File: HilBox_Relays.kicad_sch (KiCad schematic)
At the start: 49 parts, among them J9 Conn_01x10_Pin, K1 G5NB, K2 G5NB, K3 G5NB, K4 G5NB, K5 G5NB, Q10 BC847BS, Q11 BC847BS, Q12 BC847BS, Q8 BC847BS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

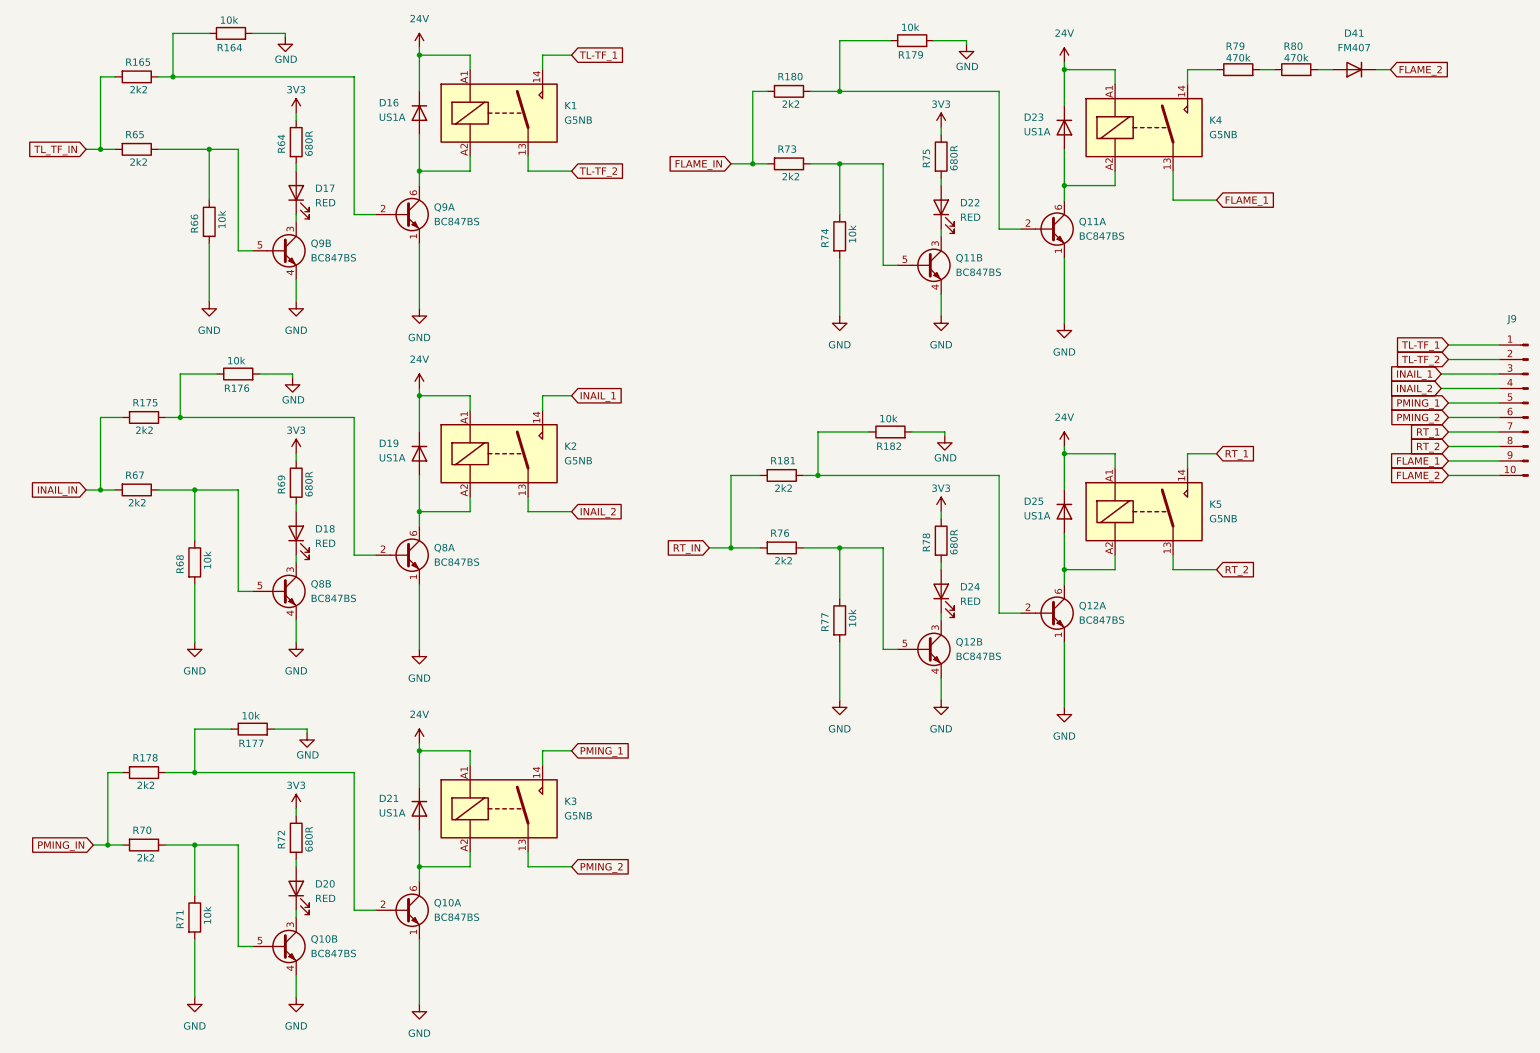
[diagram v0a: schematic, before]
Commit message: Modification in half of target
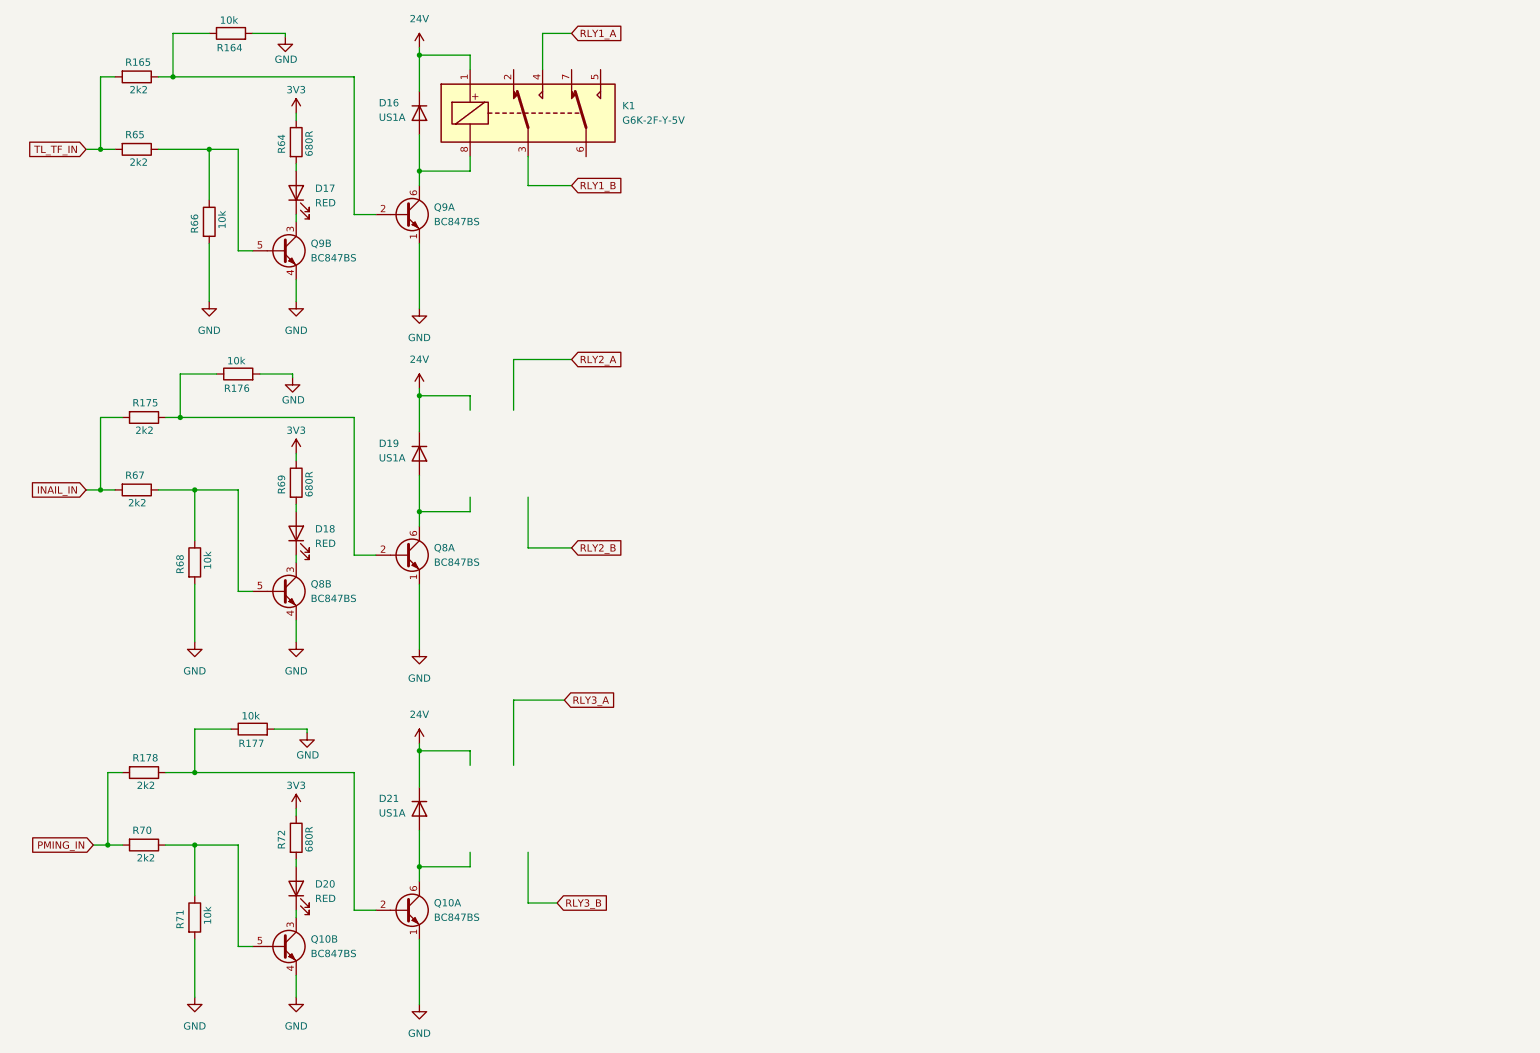
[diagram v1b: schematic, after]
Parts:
- removed D22, D24: RED, LED_SMD:LED_1206_3216Metric, symbol Device:LED
- removed D23, D25: US1A, Diode_SMD:D_SMA, symbol Diode:US1A
- removed D41: FM407, Diode_SMD:D_SMA, symbol Device:D
- removed J9: Conn_01x10_Pin, Gascard_Lib:Terminal_Block_3_81_10p, symbol Connector:Conn_01x10_Pin
- removed K1, K2, K3, K4, K5: G5NB, Relay_THT:Relay_SPST_Omron_G5NB, symbol Relay:G5NB
- removed Q11, Q12: BC847BS, Package_TO_SOT_SMD:SOT-363_SC-70-6, symbol Transistor_BJT:BC847BS
- removed R179, R182, R74, R77: 10k, Resistor_SMD:R_0603_1608Metric, symbol Device:R
- removed R180, R181, R73, R76: 2k2, Resistor_SMD:R_0603_1608Metric, symbol Device:R
- removed R75, R78: 680R, Resistor_SMD:R_0603_1608Metric, symbol Device:R
- removed R79, R80: 470k, Resistor_SMD:R_1206_3216Metric, symbol Device:R
- added K1: G6K-2F-Y-5V, Relays:RELAY_G6K-2F_DC5, symbol Relay:G6K-2
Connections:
- net 24V: now also K1.1
- net at D16.2 (A), Q9.6 (C1): now also K1.8
- new net RLY1_A: K1.4
- new net RLY1_B: K1.3

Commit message: Schematic design at finish
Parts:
- added K2, K3: G6K-2F-Y-5V, Relays:RELAY_G6K-2F_DC5, symbol Relay:G6K-2
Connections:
- net 24V: now also K2.1, K3.1
- net RLY2_A: now also K2.2
- net RLY2_B: now also K2.3
- net RLY3_A: now also K3.2
- net RLY3_B: now also K3.3
- net at D19.2 (A), Q8.6 (C1): now also K2.8
- net at D21.2 (A), Q10.6 (C1): now also K3.8
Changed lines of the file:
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@@
+	)
+	(symbol
+		(lib_id "Relay:G6K-2")
+		(at 100.33 90.17 0)
+		(unit 1)
+		(exclude_from_sim no)
+		(in_bom yes)
+		(on_board yes)
+		(dnp no)
+		(fields_autoplaced yes)
+		(property "Reference" "K2"
+			(at 116.84 88.8999 0)
+			(effects
+				(font
+					(size 1.27 1.27)
+				)
+				(justify left)
+			)
+		)
+		(property "Value" "G6K-2F-Y-5V"
+			(at 116.84 91.4399 0)
+			(effects
+				(font
+					(size 1.27 1.27)
+				)
+				(justify left)
+			)
+		)
+		(property "Footprint" "Relays:RELAY_G6K-2F_DC5"
+			(at 100.33 90.17 0)
+			(effects
+				(font
+					(size 1.27 1.27)
+				)
+				(justify left)
+				(hide yes)
+			)
+		)
+		(property "Datasheet" "http://omronfs.omron.com/en_US/ecb/products/pdf/en-g6k.pdf"
+			(at 100.33 90.17 0)
+			(effects
+				(font
+					(size 1.27 1.27)
+				)
+				(hide yes)
+			)
+		)
+		(property "Description" "Miniature 2-pole relay, Single-side Stable"
+			(at 100.33 90.17 0)
+			(effects
+				(font
+					(size 1.27 1.27)
+				)
+				(hide yes)
+			)
+		)
+		(property "JLC_PN" "C2906368"
+			(at 100.33 90.17 0)
+			(effects
+				(font
+					(size 1.27 1.27)
+				)
+				(hide yes)
+			)
+		)
+		(pin "2"
+		)
+		(pin "3"
+		)
+		(pin "1"
+		)
+		(pin "7"
+		)
+		(pin "8"
+		)
+		(pin "4"
+		)
+		(pin "6"
+		)
+		(pin "5"
+		)
+		(instances
+			(project "HilBox"
+				(path "/c950b3bb-3e52-4d0d-8bbf-240895efa80b/f996dd68-0c02-4f61-a894-5fc7c316be5e"
+					(reference "K2")
+					(unit 1)
+				)
+			)
+		)
 	)
 	(symbol
@@
 					(unit 1)
 				)
+			)
+		)
+	)
+	(symbol
+		(lib_id "Relay:G6K-2")
+		(at 100.33 152.4 0)
+		(unit 1)
+		(exclude_from_sim no)
+		(in_bom yes)
+		(on_board yes)
+		(dnp no)
+		(fields_autoplaced yes)
+		(property "Reference" "K3"
+			(at 116.84 151.1299 0)
+			(effects
+				(font
+					(size 1.27 1.27)
+				)
+				(justify left)
+			)
+		)
+		(property "Value" "G6K-2F-Y-5V"
+			(at 116.84 153.6699 0)
+			(effects
+				(font
+					(size 1.27 1.27)
+				)
+				(justify left)
+			)
+		)
+		(property "Footprint" "Relays:RELAY_G6K-2F_DC5"
+			(at 100.33 152.4 0)
+			(effects
+				(font
+					(size 1.27 1.27)
+				)
+				(justify left)
+				(hide yes)
+			)
+		)
+		(property "Datasheet" "http://omronfs.omron.com/en_US/ecb/products/pdf/en-g6k.pdf"
+			(at 100.33 152.4 0)
+			(effects
+				(font
+					(size 1.27 1.27)
+				)
+				(hide yes)
+			)
+		)
+		(property "Description" "Miniature 2-pole relay, Single-side Stable"
+			(at 100.33 152.4 0)
+			(effects
+				(font
+					(size 1.27 1.27)
+				)
+				(hide yes)
+			)
+		)
+		(property "JLC_PN" "C2906368"
+			(at 100.33 152.4 0)
+			(effects
+				(font
+					(size 1.27 1.27)
+				)
+				(hide yes)
+			)
+		)
+		(pin "2"
+		)
+		(pin "3"
+		)
+		(pin "1"
+		)
+		(pin "7"
+		)
+		(pin "8"
+		)
+		(pin "4"
+		)
+		(pin "6"
+		)
+		(pin "5"
+		)
+		(instances
+			(project "HilBox"
+				(path "/c950b3bb-3e52-4d0d-8bbf-240895efa80b/f996dd68-0c02-4f61-a894-5fc7c316be5e"
+					(reference "K3")
+					(unit 1)
+				)

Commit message: Layout 90% done
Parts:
- removed D17, D18, D20: RED, LED_SMD:LED_1206_3216Metric, symbol Device:LED
- added D12, D14, D15, D3: RED, LED_SMD:LED_0603_1608Metric, symbol Device:LED
- added D4: BAT46W, Diode_SMD:D_SOD-123, symbol Diode:US1A
- added K4: G6K-2F-Y-24V, Relays:RELAY_G6K-2F_DC5, symbol Relay:G6K-2
- added Q3: BC847BS, Package_TO_SOT_SMD:SOT-363_SC-70-6, symbol Transistor_BJT:BC847BS
- added R10, R11: 10k, Resistor_SMD:R_0603_1608Metric, symbol Device:R
- added R12: 680R, Resistor_SMD:R_0603_1608Metric, symbol Device:R
- added R8, R9: 2k2, Resistor_SMD:R_0603_1608Metric, symbol Device:R
- D16, D19, D21: value US1A -> BAT46W; footprint Diode_SMD:D_SMA -> Diode_SMD:D_SOD-123; JLC_PN C232824 -> C83152
- K1, K2, K3: value G6K-2F-Y-5V -> G6K-2F-Y-24V; JLC_PN C2906368 -> C5278023
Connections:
- net 24V: now also D4.1 (K), K4.1
- net 3V3: now also R12.1
- net GND: now also Q3.1 (E1), Q3.4 (E2), R10.2, R11.2
- net PMING_IN: now also R8.2, R9.2
- net RLY3_A: now also K4.2
- net RLY3_B: now also K4.3
- net at Q9.3 (C2): now also D3.1 (K)
- net at R64.2: now also D3.2 (A)
- net at R69.2: now also D12.2 (A)
- net at R72.2: now also D14.2 (A)
- net at Q8.3 (C2): now also D12.1 (K)
- net at Q10.3 (C2): now also D14.1 (K)
- new net: D15.1 (K), Q3.3 (C2)
- new net: D15.2 (A), R12.2
- new net: Q3.5 (B2), R10.1, R9.1
- new net: Q3.2 (B1), R11.1, R8.1
- new net: D4.2 (A), K4.8, Q3.6 (C1)

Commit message: Gate finalized! PCB ordered
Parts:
- R10, R66, R68, R71: value 10k -> 100k; JLC_PN C25804 -> C15458
- R12, R64, R69, R72: value 680R -> 22k; JLC_PN C25177 -> C23344
- R65, R67, R70, R9: value 2k2 -> 10k; JLC_PN C4190 -> C25804
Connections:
- net 3V3 is gone; now on net Vin: R12.1, R64.1, R69.1, R72.1
- net PMING_IN: no longer R8.2, R9.2
- net RLY1_A: now also K1.3; no longer K1.4
- net RLY1_B: now also K1.4; no longer K1.3
- net RLY2_A: now also K2.3; no longer K2.2
- net RLY2_B: now also K2.4; no longer K2.3
- net RLY3_A: now also K3.3; no longer K3.2, K4.2
- net RLY3_B: now also K3.4; no longer K3.3, K4.3
- net RLY4_B: now reaches K4.4
- net 24V renamed Vin
- new net RLY4_A: K4.3
- new net RT_IN: R8.2, R9.2
